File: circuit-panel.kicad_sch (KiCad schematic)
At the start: 49 parts, among them Q1 BC547, Q2 BC547, U1 CD40106BPWR, U2 4017, U3 CD40106BPWR, U4 NE555P, U5 CD40106BPWR, U7 CD40106BPWR

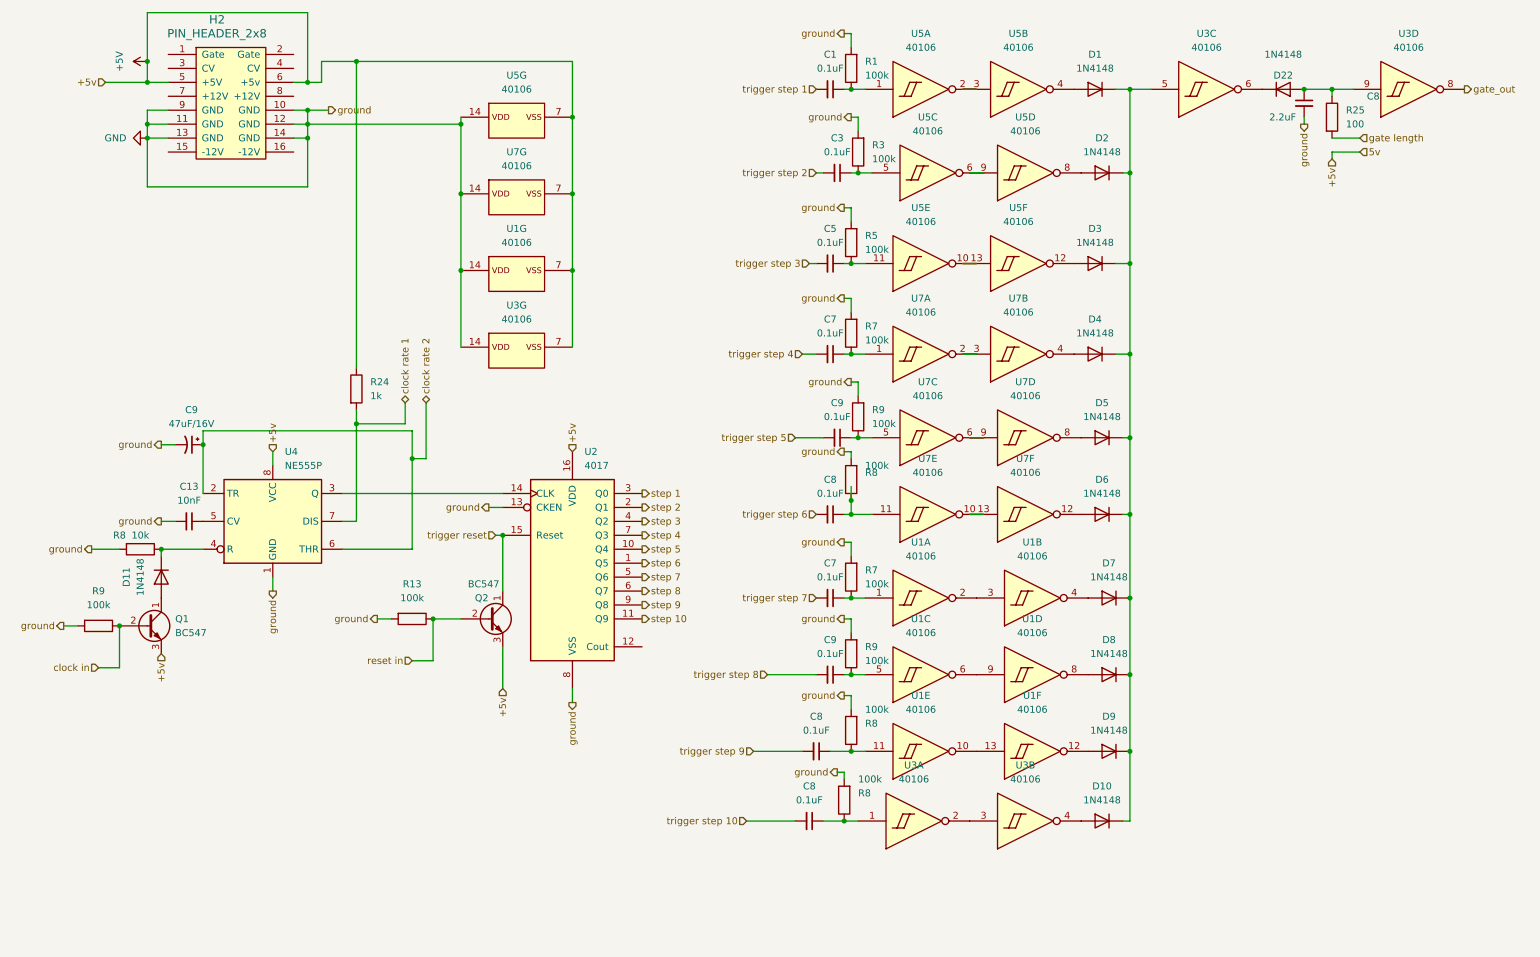
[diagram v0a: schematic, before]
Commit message: Fixed critical routing bugs
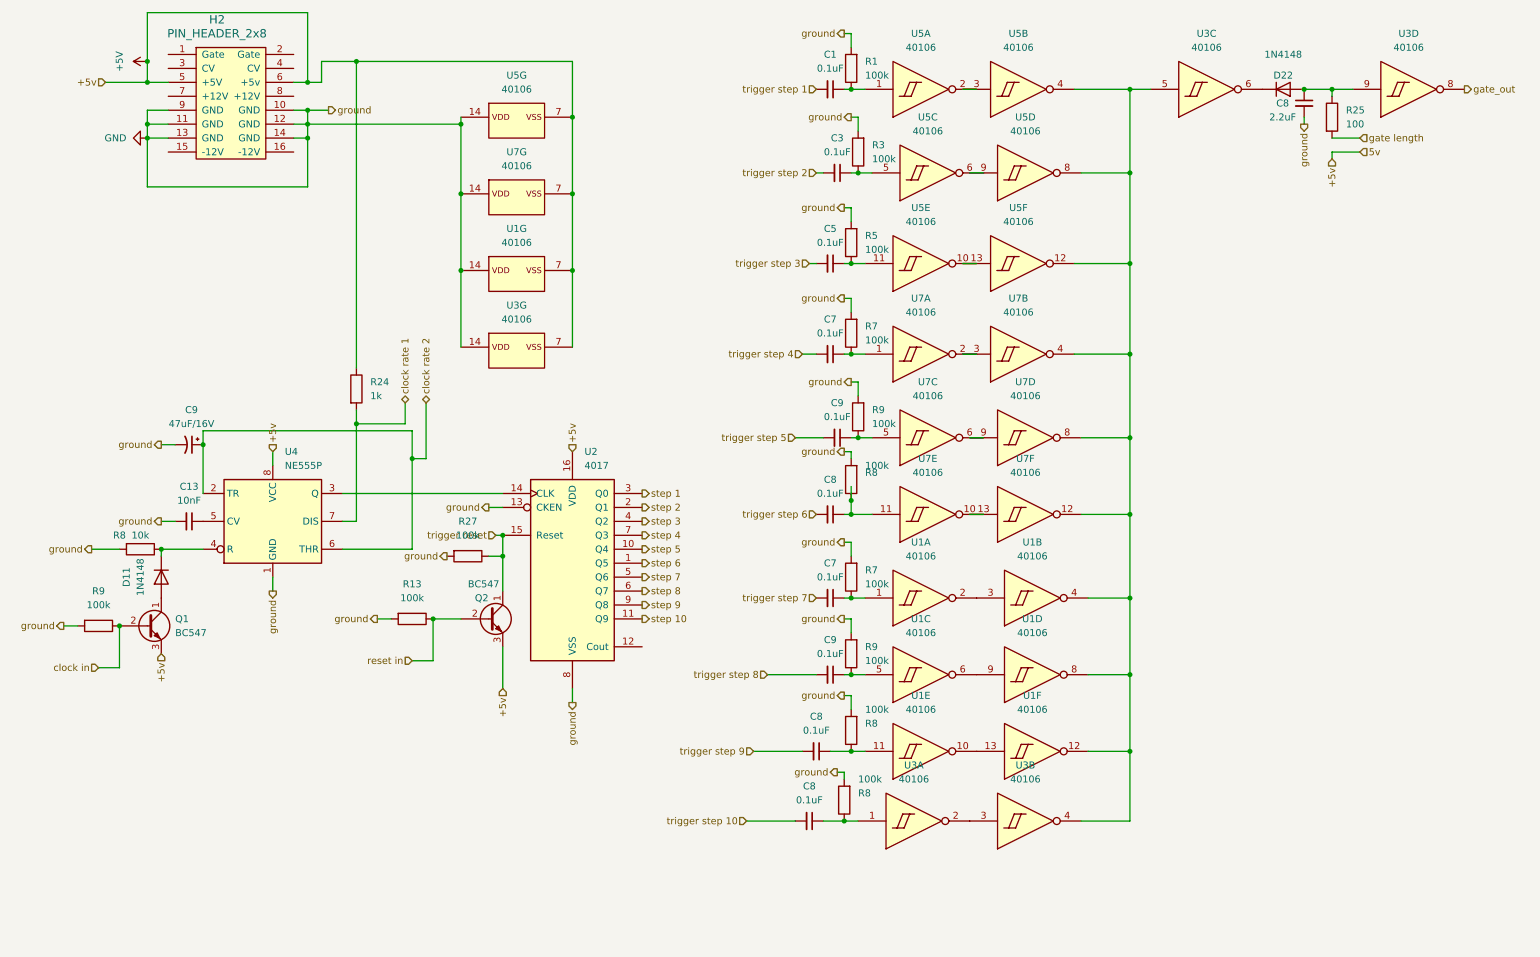
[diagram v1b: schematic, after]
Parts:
- removed D1, D10, D2, D3, D4, D5, D6, D7, D8, D9: 1N4148, Diode_THT:D_DO-35_SOD27_P7.62mm_Horizontal, symbol Diode:1N4148
- added R27: 100k_0603, Resistor_THT:R_Axial_DIN0207_L6.3mm_D2.5mm_P7.62mm_Horizontal, symbol PCM_4ms_Resistor:100k_0603
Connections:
- net GND: now also R27.2
- net trigger reset: now also R27.1
- net at U3.5 (I): now also U1.12 (O), U1.4 (O), U1.8 (O), U3.4 (O), U5.12 (O), U5.4 (O), U5.8 (O), U7.12 (O), U7.4 (O), U7.8 (O)

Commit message: Version 1.3 of the model.
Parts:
- added Q3: BC547, Package_TO_SOT_THT:TO-92_Inline, symbol Transistor_BJT:BC547
- added R28: 10k_0603, Resistor_THT:R_Axial_DIN0207_L6.3mm_D2.5mm_P7.62mm_Horizontal, symbol PCM_4ms_Resistor:10k_0603
- added R30: 100k_0603, Resistor_THT:R_Axial_DIN0207_L6.3mm_D2.5mm_P7.62mm_Horizontal, symbol PCM_4ms_Resistor:100k_0603
- added unit 6 of U3
- added unit 5 of U3
- renumbered C7 to C1, C7 to C10, C8 to C11, C9 to C12, C1 to C2, C8 to C3, C3 to C4, C9 to C5, C5 to C6, C8 to C7, R7 to R1, R7 to R10, R8 to R11, R9 to R12, R1 to R2, R8 to R3, R3 to R4, R9 to R5, R5 to R6, R8 to R7, U5 to U6, U7 to U8
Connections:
- net +5V: now also U1.14 (VDD), U3.14 (VDD), U6.14 (VDD), U8.14 (VDD), Q3.1 (C); no longer U1.7 (VSS), U3.7 (VSS), U6.7 (VSS), U8.7 (VSS)
- net GND: now also U1.7 (VSS), U3.7 (VSS), U6.7 (VSS), U8.7 (VSS), R28.2, R30.2; no longer U1.14 (VDD), U3.14 (VDD), U6.14 (VDD), U8.14 (VDD)
- net gate_out: now also Q3.3 (E), R28.1; no longer U3.8 (O)
- net at U1.12 (O), U1.4 (O), U1.8 (O)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: now also U3.12 (O)
- new net: Q3.2 (B), U3.8 (O)
- new net: R30.1, U3.11 (I)
- new net: U3.10 (O), U3.13 (I)
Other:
- moved on the sheet: U3D
